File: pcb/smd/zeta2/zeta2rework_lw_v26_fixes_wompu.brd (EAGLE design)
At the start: 81 x 45.7 mm, 80 parts, among them U5 DS18B20U+

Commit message: version 3 of pcb should be finihsed now
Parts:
- removed BOOTCONFIG: (no value), special:EDG-02
- removed C11, C18, C21: 0.1µF, rcl:C1206
- removed C20: 10nf, rcl:C1206
- removed IRLML1, IRLML2502: (no value), zetex:SOT-23
- removed MPU6050: MPU-6050, MPU-6050:QFN50P400X400X95-24N
- removed Q9: (no value), semicon-smd-ipc:SOT23
- removed R11, R15: 132k, rcl:R0603
- removed R18: 500, rcl:R0603
- removed SCL, SDA: TPSQTP20R, testpad:TP20R
- added 1.8V_CONV: MCP1700T-1802E/TT, MCP1700T-2102E_TT:SOT95P237X112-3N
- added C1: 100nF, rcl:C1206
- added C14: 1µF, rcl:C1206
- added C6, C7, C8: 0.1nF, rcl:C1206
- added J1: B4B-ZR(LF)(SN), B4B-ZR(LF)(SN):SHDR4W50P0X150_1X4_750X350X450
- added M1, M2, M3: IRLML2502, IRLML2502TRPBF:SOT23
- added R1, R2: 10k, rcl:R0603
- added R6: 22R, rcl:R0603
- added U3: ICM-20948, ICM-20948:QFN40P300X300X105-25N
- C10, C12, C3, C34, C43: device rcl:UD-4X5,8_NICHICON -> rcl:UD-5X5,8_NICHICON
- C17: value 2,2nF -> 1µF
- R10, R12, R14, R4, R7, R8: value 100k -> 10k
- R3: value 220R -> 0R
- moved 3.3V 12.7 mm to (13.3, 31.8)
- moved GND 12.3 mm to (13.3, 35.6)
- moved R29 12.1 mm to (12.3, 30.3), turned to 0 degrees
- moved C17 11.3 mm to (41.9, 37.5), turned to 90 degrees
- moved R20 8.19 mm to (15.6, 30.3), turned to 180 degrees
- moved C37 5.46 mm to (22.6, 36.0), turned to 0 degrees
- moved C3 4.76 mm to (39.9, 18.2)
- moved R12 4.49 mm to (48.3, 31.1), turned to 90 degrees
- moved C39 4.26 mm to (39.4, 22.9), turned to 0 degrees
- moved R14 3.49 mm to (52.3, 31.1), turned to 90 degrees
- moved R30 3.08 mm to (26.8, 37.4)
- moved R35 2.52 mm to (1.88, 31.8), turned to 270 degrees
- moved R8 2.36 mm to (50.3, 31.1), turned to 90 degrees
- moved KX-9A 1.91 mm to (22.2, 32.4), turned to 0 degrees
- moved C23 1.27 mm to (5.41, 28.6)
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- renumbered 3.3V_CONF to 3.3V_CONV
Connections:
- removed net BOOT0: BOOTCONFIG.2, R15.2, STM32F103CB.44
- removed net BOOT1: BOOTCONFIG.1, R11.2, STM32F103CB.20
- removed net BOOT2: RPI_ZERO.29
- removed net BOOT3: RPI_ZERO.27
- removed net MPU_INT: MPU6050.12
- removed net N$19: Q9.1, R18.2
- removed net N$20: Q9.2, R3.1
- removed net N$34: C17.1, MPU6050.20
- removed net N$36: C21.1, MPU6050.10
- new net +1.8V: 1.8V_CONV.2, C14.1, C8.1, U3.8
- new net INT_MD_1: J1.3, STM32F103CB.21
- new net INT_MD_2: J1.2, STM32F103CB.22
- new net N$10: M3.1, R6.2
- new net N$5: R1.1, STM32F103CB.44
- new net N$8: C7.1, U3.10
- new net N$9: FRONTLIGHT.P2, M3.3
- net +3V3: now also 1.8V_CONV.3, C17.1, C6.1, R2.2, U3.13; no longer BOOTCONFIG.3, BOOTCONFIG.4, C18.1, C20.1, MPU6050.13, MPU6050.8
- net +5V: now also 3.3V_CONV.3, C15.1, J1.4, R3.1; no longer C11.1, Q9.3
- net +8V: no longer 3.3V_CONV.3, C15.1
- net FRONT_LIGHT: now also R6.1; no longer R18.1
- net GND: now also 1.8V_CONV.1, C1.2, C14.2, C6.2, C7.2, C8.2, J1.1, M1.2, M2.2, M3.2, R1.2, U3.18; no longer C11.2, C18.2, C20.2, C21.2, FRONTLIGHT.P2, IRLML1.2, IRLML2502.2, MPU6050.1, MPU6050.11, MPU6050.18, MPU6050.9, R11.1, R15.1
- net N$37: now also M2.1; no longer IRLML2502.3
- net N$38: now also M1.1; no longer IRLML1.3
- net N$39: now also M1.3; no longer IRLML1.1
- net N$55: now also M2.3; no longer IRLML2502.1
- net NRST: now also C1.1, R2.1
- net SCL: now also I2C.1, U3.23; no longer I2C.2, MPU6050.23, SCL.TP
- net SDA: now also I2C.2, U3.24; no longer I2C.1, MPU6050.24, SDA.TP
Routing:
- net GND: track 634.0 -> 673.7 mm, vias 7 -> 10
- net +3V3: track 216.1 -> 186.4 mm
- net BOOT0: track 27.8 -> 0.00 mm
- net SCL: track 106.0 -> 84.6 mm, vias 4 -> 3
- net BOOT1: track 19.3 -> 0.00 mm
- net INT_MD_2: track 0.00 -> 14.9 mm
- net INT_MD_1: track 0.00 -> 14.5 mm
- net +1.8V: track 0.00 -> 14.4 mm
- net +5V: track 220.9 -> 232.3 mm, vias 1 -> 2
- net N$20: track 10.7 -> 0.00 mm
- net NRST: track 30.2 -> 39.8 mm
- net N$47: track 19.0 -> 10.4 mm
- net BAT_LVL: track 42.5 -> 49.1 mm
- net +8V: track 238.7 -> 232.8 mm
- net SDA: track 95.3 -> 90.6 mm
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- added copper zone on layer 16, net +8V
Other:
- board text added: "5v I1 I2 GND"
- board text removed: "TODO: am untersten rechten (pin24) 3.3v vom stm32 fehlt der kondensator"
- board text removed: "TODO: heatsink thermal for +3v3"

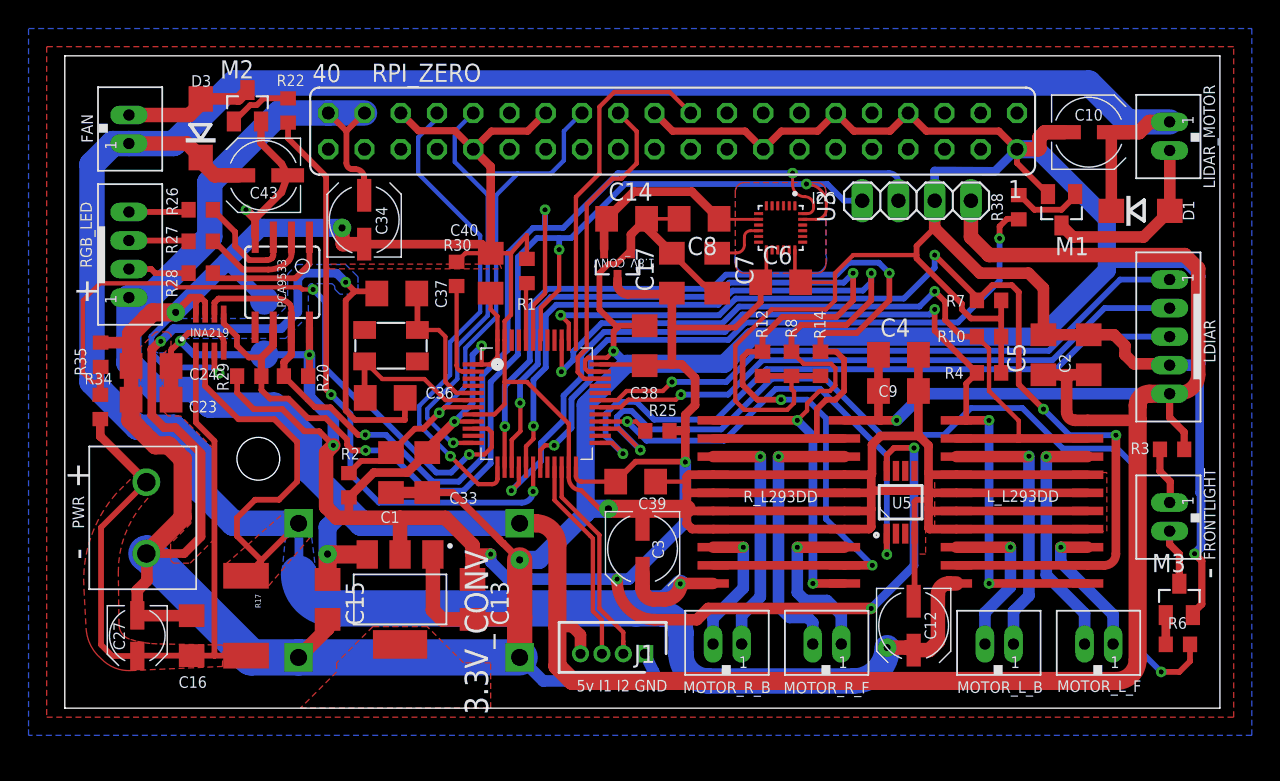
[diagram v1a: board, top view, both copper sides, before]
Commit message: moved pwr in, added smd LED
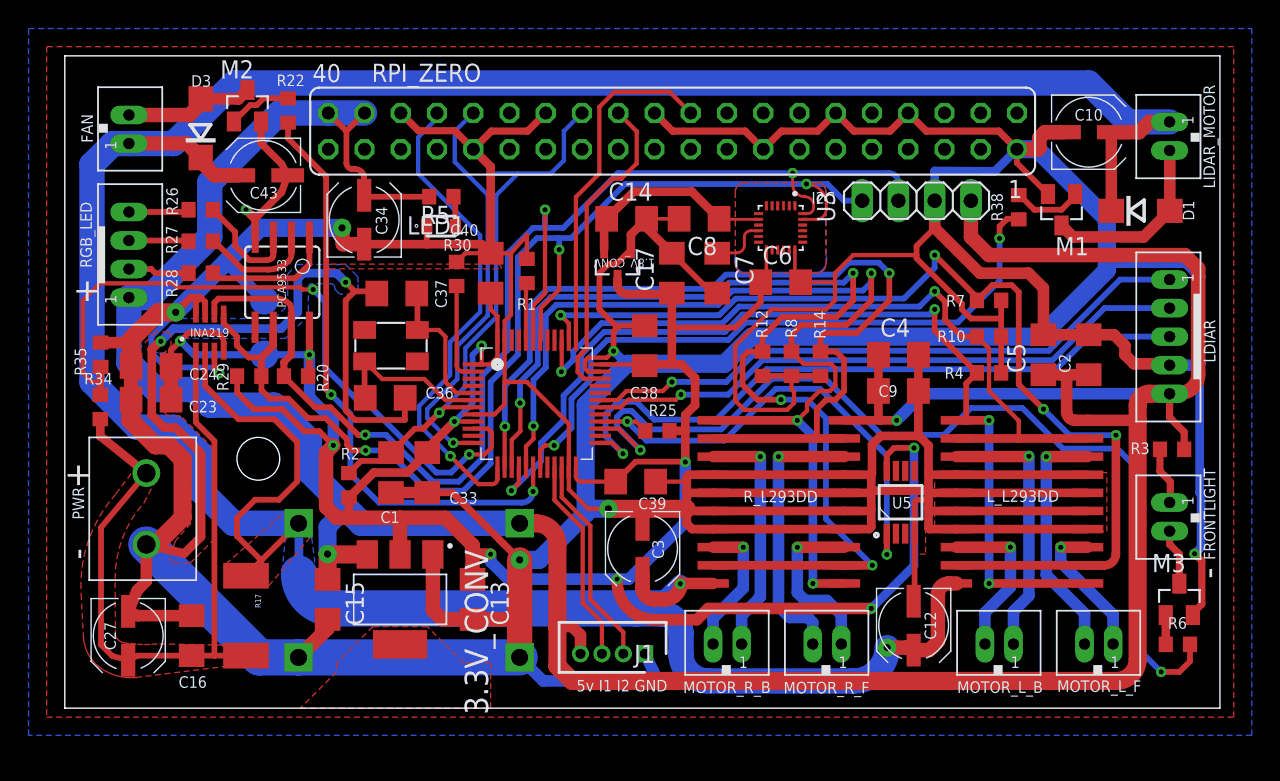
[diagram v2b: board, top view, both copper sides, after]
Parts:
- added LED1: LT M673, LT_M673-N1R2-25:LTM673-N1R2-25
- added R5: 220R, rcl:R0603
- C27: device rcl:UD-4X5,8_NICHICON -> rcl:UD-5X5,8_NICHICON
- moved C27 0.64 mm to (3.81, 12.1)
- moved PWR 0.63 mm to (5.08, 21.0)
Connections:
- new net N$7: LED1.2, R5.1
- net +5V: now also R5.2
- net GND: now also LED1.1
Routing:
- net +5V: track 232.3 -> 236.9 mm
- net GND: track 673.7 -> 676.9 mm
- net N$7: track 0.00 -> 2.11 mm
